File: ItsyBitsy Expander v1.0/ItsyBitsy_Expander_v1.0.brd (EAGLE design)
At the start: 60 x 71 mm, 45 parts, among them CN2 JSTPH, IC1 74AHC1G125, J1 H4P-SMD-2.0, J10 H4P-SMD-2.0, J11 H4P-SMD-2.0, J12 H4P-SMD-2.0, J2 H4P-SMD-2.0, J3 H4P-SMD-2.0, J4 H4P-SMD-2.0, J5 H4P-SMD-2.0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

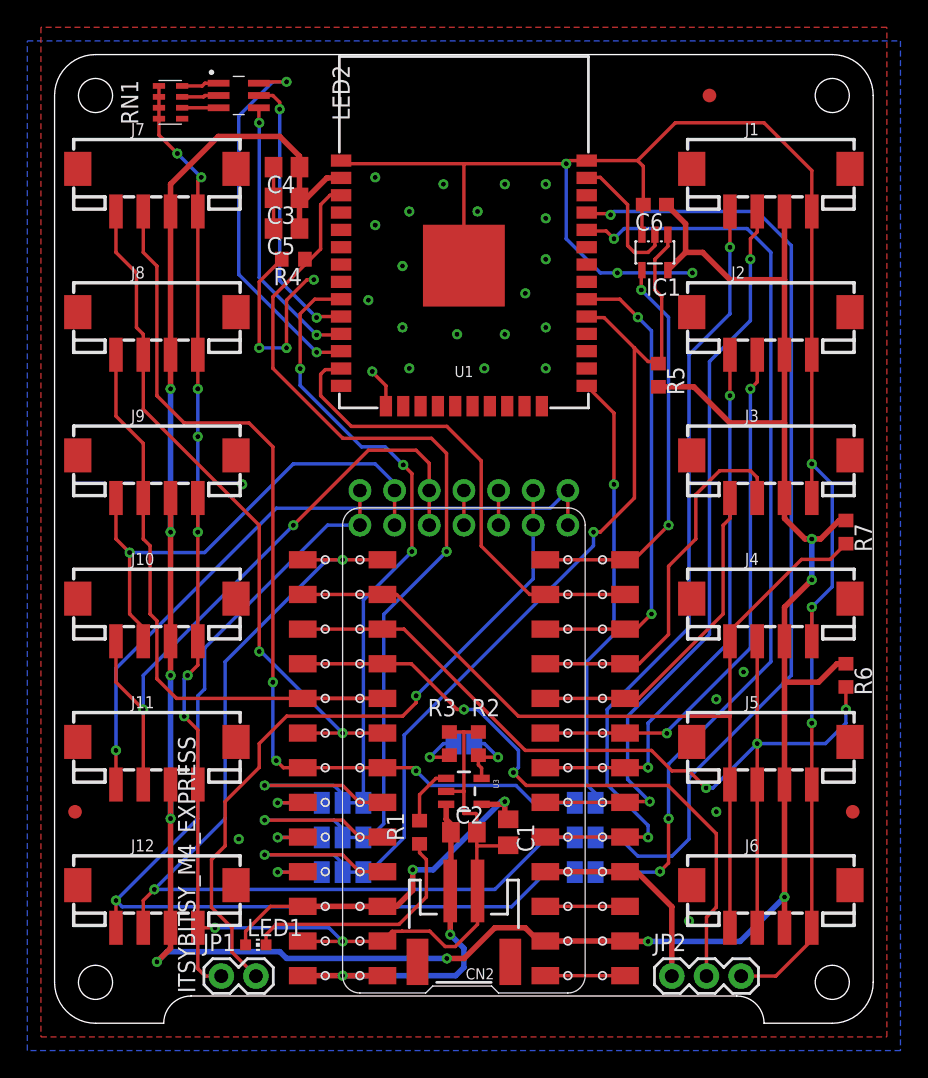
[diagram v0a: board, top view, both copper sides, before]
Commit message: Fix bug in ESP32 footprint
Flip RX and TX pads
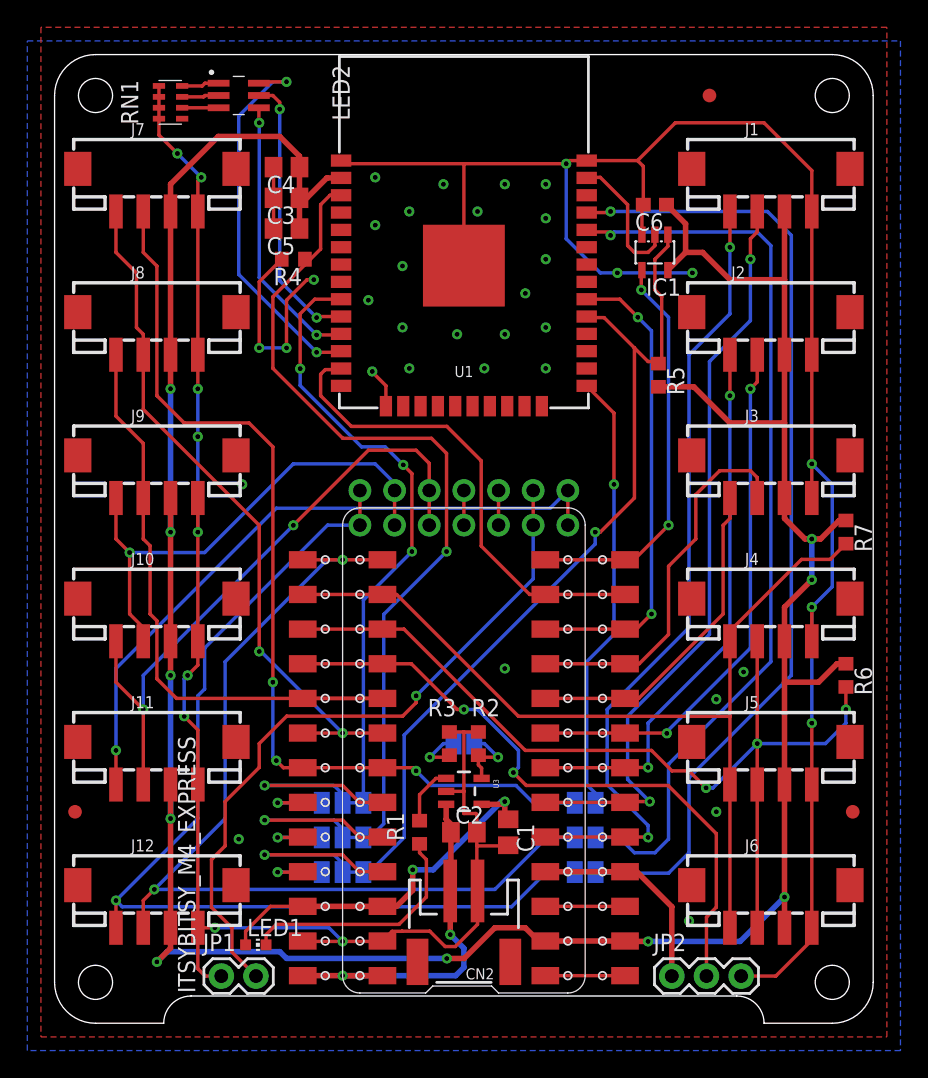
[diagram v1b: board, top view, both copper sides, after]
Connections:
- net ESP_RX: now also U1.34; no longer U1.35
- net ESP_TX: now also U1.35; no longer U1.34
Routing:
- net ESP_RX: track 70.7 -> 67.1 mm
- net ESP_TX: track 68.3 -> 71.6 mm, vias 3 -> 1
- net GND: vias 44 -> 45
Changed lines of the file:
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@@
 <setting verticaltext="up"/>
 </settings>
-<grid distance="0.5" unitdist="mm" unit="mm" style="lines" multiple="1" display="yes" altdistance="5" altunitdist="mil" altunit="mil"/>
+<grid distance="0.25" unitdist="mm" unit="mm" style="lines" multiple="1" display="yes" altdistance="5" altunitdist="mil" altunit="mil"/>
 <layers>
 <layer number="1" name="Top" color="4" fill="1" visible="yes" active="yes"/>
@@
 <wire x1="27" y1="33.5" x2="27" y2="26" width="0.254" layer="16"/>
 <wire x1="27" y1="26" x2="25.5" y2="24.5" width="0.254" layer="16"/>
+<via x="3" y="20" extent="1-16" drill="0.35"/>
 </signal>
 <signal name="CHG">
@@
 <wire x1="9" y1="45.8" x2="9.08" y2="45.72" width="0.254" layer="1"/>
 <wire x1="10.28" y1="45.72" x2="9.08" y2="45.72" width="0.254" layer="1"/>
-<via x="9.5" y="30" extent="1-16" drill="0.35"/>
+<via x="9.625" y="30" extent="1-16" drill="0.35"/>
 <wire x1="14.5" y1="47.25" x2="14.5" y2="42.6" width="0.254" layer="1"/>
 <wire x1="14.25" y1="42.35" x2="14.5" y2="42.6" width="0.254" layer="1"/>
 <wire x1="12.5" y1="43.5" x2="12.5" y2="32.5" width="0.254" layer="1"/>
 <wire x1="12.5" y1="32.5" x2="10" y2="30" width="0.254" layer="1"/>
-<wire x1="9.5" y1="30" x2="10" y2="30" width="0.254" layer="1"/>
+<wire x1="9.625" y1="30" x2="10" y2="30" width="0.254" layer="1"/>
 <wire x1="12.5" y1="43.5" x2="10.28" y2="45.72" width="0.254" layer="1"/>
 <wire x1="12.5" y1="43.5" x2="13.5" y2="42.5" width="0.254" layer="1"/>
@@
 <wire x1="-4.375" y1="15.125" x2="-4.375" y2="7.625" width="0.254" layer="16"/>
 <wire x1="-7" y1="5" x2="-4.375" y2="7.625" width="0.254" layer="16"/>
-<wire x1="9.5" y1="30" x2="9.5" y2="29" width="0.254" layer="16"/>
-<wire x1="9.5" y1="29" x2="-4.375" y2="15.125" width="0.254" layer="16"/>
+<wire x1="9.625" y1="30" x2="9.625" y2="29.125" width="0.254" layer="16"/>
+<wire x1="9.625" y1="29.125" x2="-4.375" y2="15.125" width="0.254" layer="16"/>
 <wire x1="-7.366" y1="5.08" x2="-7.08" y2="5.08" width="0.254" layer="16"/>
 <wire x1="-7.08" y1="5.08" x2="-7" y2="5" width="0.254" layer="16"/>
@@
 </signal>
 <signal name="ESP_RX">
-<contactref element="U1" pad="35"/>
+<contactref element="U1" pad="34"/>
 <contactref element="SJ6" pad="1"/>
-<wire x1="9" y1="53.42" x2="9.08" y2="53.34" width="0.254" layer="1"/>
-<wire x1="10.66" y1="53.34" x2="10.75" y2="53.25" width="0.254" layer="1"/>
-<wire x1="10.66" y1="53.34" x2="9.08" y2="53.34" width="0.254" layer="1"/>
-<via x="10.75" y="53.25" extent="1-16" drill="0.35"/>
-<wire x1="21.5" y1="53.5" x2="11" y2="53.5" width="0.254" layer="16"/>
-<wire x1="10.75" y1="53.25" x2="11" y2="53.5" width="0.254" layer="16"/>
-<wire x1="24" y1="51" x2="21.5" y2="53.5" width="0.254" layer="16"/>
-<wire x1="24" y1="19.5" x2="24" y2="51" width="0.254" layer="16"/>
-<wire x1="15.25" y1="6.25" x2="12.75" y2="6.25" width="0.254" layer="16"/>
-<wire x1="15.25" y1="6.25" x2="16.5" y2="7.5" width="0.254" layer="16"/>
-<wire x1="11.38" y1="7.62" x2="9.652" y2="7.62" width="0.254" layer="16"/>
-<wire x1="12.75" y1="6.25" x2="11.38" y2="7.62" width="0.254" layer="16"/>
-<wire x1="16.5" y1="12" x2="24" y2="19.5" width="0.254" layer="16"/>
-<wire x1="16.5" y1="7.5" x2="16.5" y2="12" width="0.254" layer="16"/>
+<wire x1="9.652" y1="7.62" x2="11.38" y2="7.62" width="0.254" layer="16"/>
+<wire x1="11.38" y1="7.62" x2="12.5" y2="6.5" width="0.254" layer="16"/>
+<wire x1="12.5" y1="6.5" x2="14" y2="6.5" width="0.254" layer="16"/>
+<wire x1="14" y1="6.5" x2="15" y2="7.5" width="0.254" layer="16"/>
+<wire x1="15" y1="7.5" x2="15" y2="13" width="0.254" layer="16"/>
+<wire x1="15" y1="13" x2="22.5" y2="20.5" width="0.254" layer="16"/>
+<wire x1="22.5" y1="51" x2="21.5" y2="52" width="0.254" layer="16"/>
+<wire x1="22.5" y1="20.5" x2="22.5" y2="51" width="0.254" layer="16"/>
+<wire x1="21.5" y1="52" x2="11" y2="52" width="0.254" layer="16"/>
+<wire x1="11" y1="52" x2="10.75" y2="51.75" width="0.254" layer="16"/>
+<via x="10.75" y="51.75" extent="1-16" drill="0.35"/>
+<wire x1="10.75" y1="51.75" x2="10.75" y2="51.9" width="0.254" layer="1"/>
+<wire x1="10.75" y1="51.9" x2="10.65" y2="52" width="0.254" layer="1"/>
+<wire x1="10.65" y1="52" x2="9.15" y2="52" width="0.254" layer="1"/>
+<wire x1="9.15" y1="52" x2="9" y2="52.15" width="0.254" layer="1"/>
 </signal>
 <signal name="ESP_MISO">
@@
 <signal name="ESP_TX">
 <contactref element="SJ5" pad="1"/>
-<contactref element="U1" pad="34"/>
-<wire x1="9" y1="52.15" x2="9.08" y2="52.07" width="0.254" layer="1"/>
-<wire x1="9.08" y1="52.07" x2="10.43" y2="52.07" width="0.254" layer="1"/>
-<wire x1="10.43" y1="52.07" x2="11" y2="51.5" width="0.254" layer="1"/>
-<via x="11" y="51.5" extent="1-16" drill="0.35"/>
-<wire x1="11" y1="51.5" x2="11.75" y2="52.25" width="0.254" layer="16"/>
-<wire x1="11.75" y1="52.25" x2="20.75" y2="52.25" width="0.254" layer="16"/>
-<wire x1="15" y1="13" x2="15" y2="9" width="0.254" layer="16"/>
-<wire x1="20.75" y1="52.25" x2="22.5" y2="50.5" width="0.254" layer="16"/>
-<wire x1="22.5" y1="50.5" x2="22.5" y2="20.5" width="0.254" layer="16"/>
-<wire x1="22.5" y1="20.5" x2="15" y2="13" width="0.254" layer="16"/>
-<via x="15" y="9" extent="1-16" drill="0.35"/>
-<wire x1="15" y1="9" x2="15" y2="5.75" width="0.254" layer="1"/>
-<wire x1="15" y1="5.75" x2="14.375" y2="5.125" width="0.254" layer="1"/>
-<via x="14.375" y="5.125" extent="1-16" drill="0.35"/>
-<wire x1="14.375" y1="5.125" x2="14.33" y2="5.08" width="0.254" layer="16"/>
-<wire x1="14.33" y1="5.08" x2="9.652" y2="5.08" width="0.254" layer="16"/>
+<contactref element="U1" pad="35"/>
+<wire x1="15" y1="5" x2="9.732" y2="5" width="0.254" layer="16"/>
+<wire x1="9.732" y1="5" x2="9.652" y2="5.08" width="0.254" layer="16"/>
+<wire x1="10.75" y1="53.5" x2="10.58" y2="53.5" width="0.254" layer="1"/>
+<wire x1="10.58" y1="53.5" x2="10.5" y2="53.42" width="0.254" layer="1"/>
+<wire x1="9" y1="53.42" x2="10.5" y2="53.42" width="0.254" layer="1"/>
+<via x="10.75" y="53.5" extent="1-16" drill="0.35"/>
+<wire x1="24" y1="19.5" x2="24" y2="51.75" width="0.254" layer="16"/>
+<wire x1="16.5" y1="12" x2="16.5" y2="6.5" width="0.254" layer="16"/>
+<wire x1="16.5" y1="6.5" x2="15" y2="5" width="0.254" layer="16"/>
+<wire x1="24" y1="19.5" x2="16.5" y2="12" width="0.254" layer="16"/>
+<wire x1="24" y1="51.75" x2="22.25" y2="53.5" width="0.254" layer="16"/>
+<wire x1="22.25" y1="53.5" x2="10.75" y2="53.5" width="0.254" layer="16"/>
 </signal>
 <signal name="ESP_GPIO">

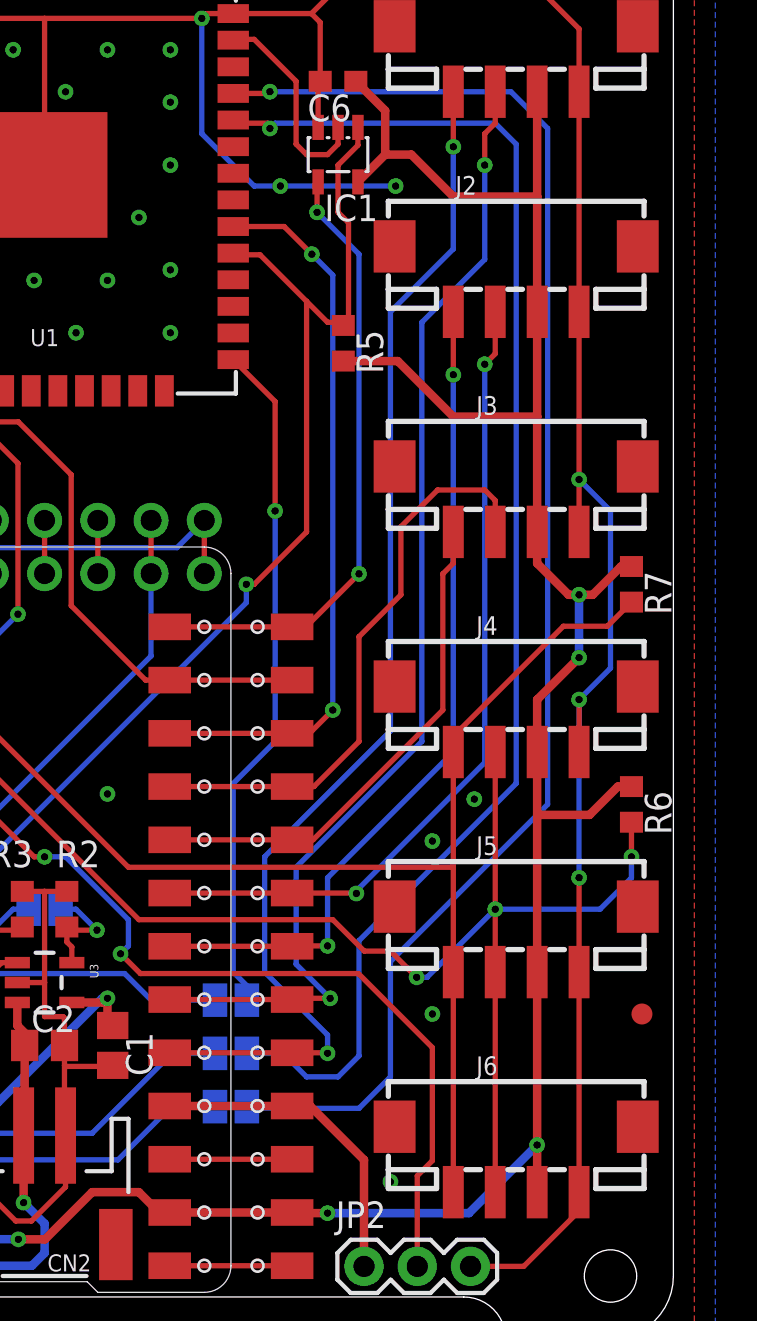
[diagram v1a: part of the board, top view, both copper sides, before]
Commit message: Upload V1.1
* Use through-hole headers
* Change CS pin for ESP32 coprocessor
* Fix bugs in previous version (Serial breakout pads for ESP32, I²C header pinout)
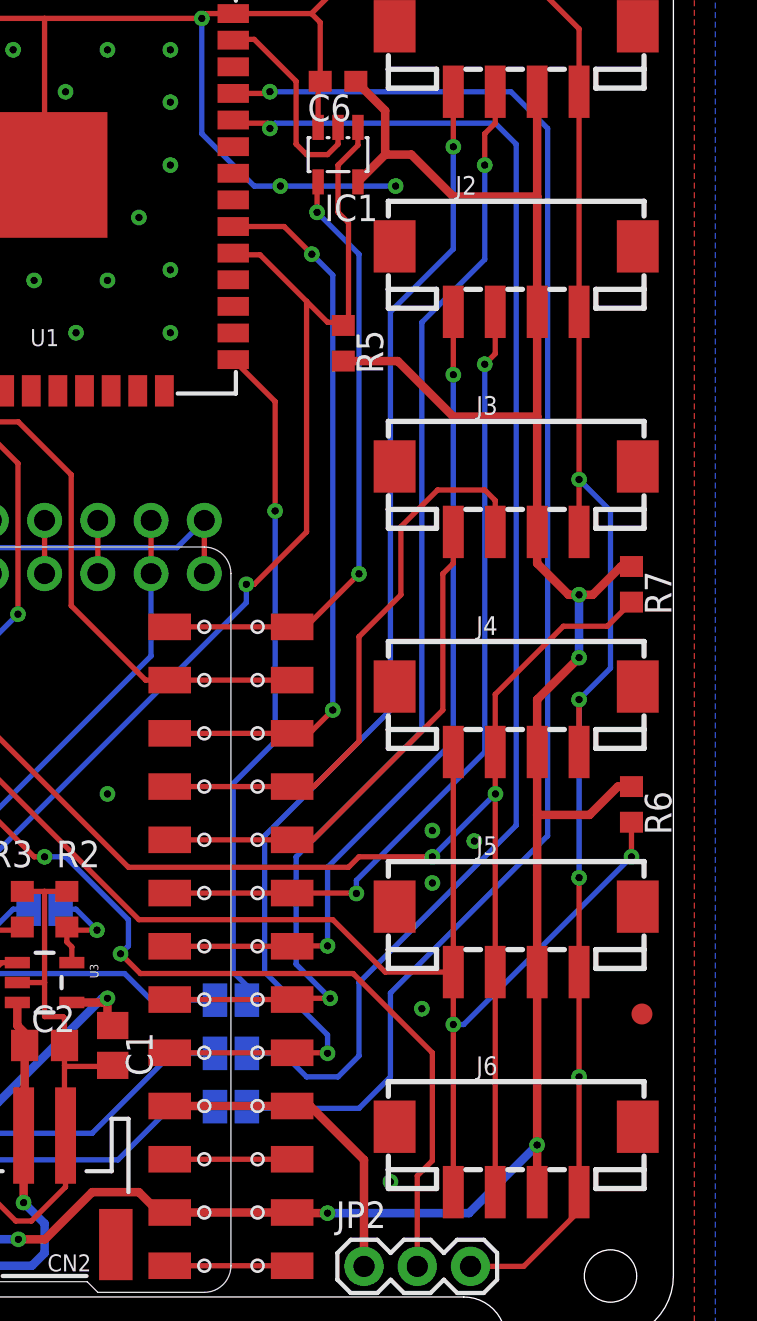
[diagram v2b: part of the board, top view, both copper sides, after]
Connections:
- net SCL: now also J4.1, J5.1, J6.1; no longer J4.2, J5.2, J6.2
- net SDA: now also J4.2, J5.2, J6.2; no longer J4.1, J5.1, J6.1
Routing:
- net SDA: track 67.9 -> 70.6 mm, vias 0 -> 2
- net SCL: track 70.2 -> 70.5 mm, vias 3 -> 2
- net GND: vias 45 -> 47
